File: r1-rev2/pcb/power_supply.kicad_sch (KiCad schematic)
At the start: 26 parts, among them J1 GT-BTP30003-xxxA-16A, Q1 AO3401A, U1 LM66100DCK, U2 TPS62A01DRLR, U3 TPS62A01DRLR, U4 TP4057, U5 XC6206P33xMR

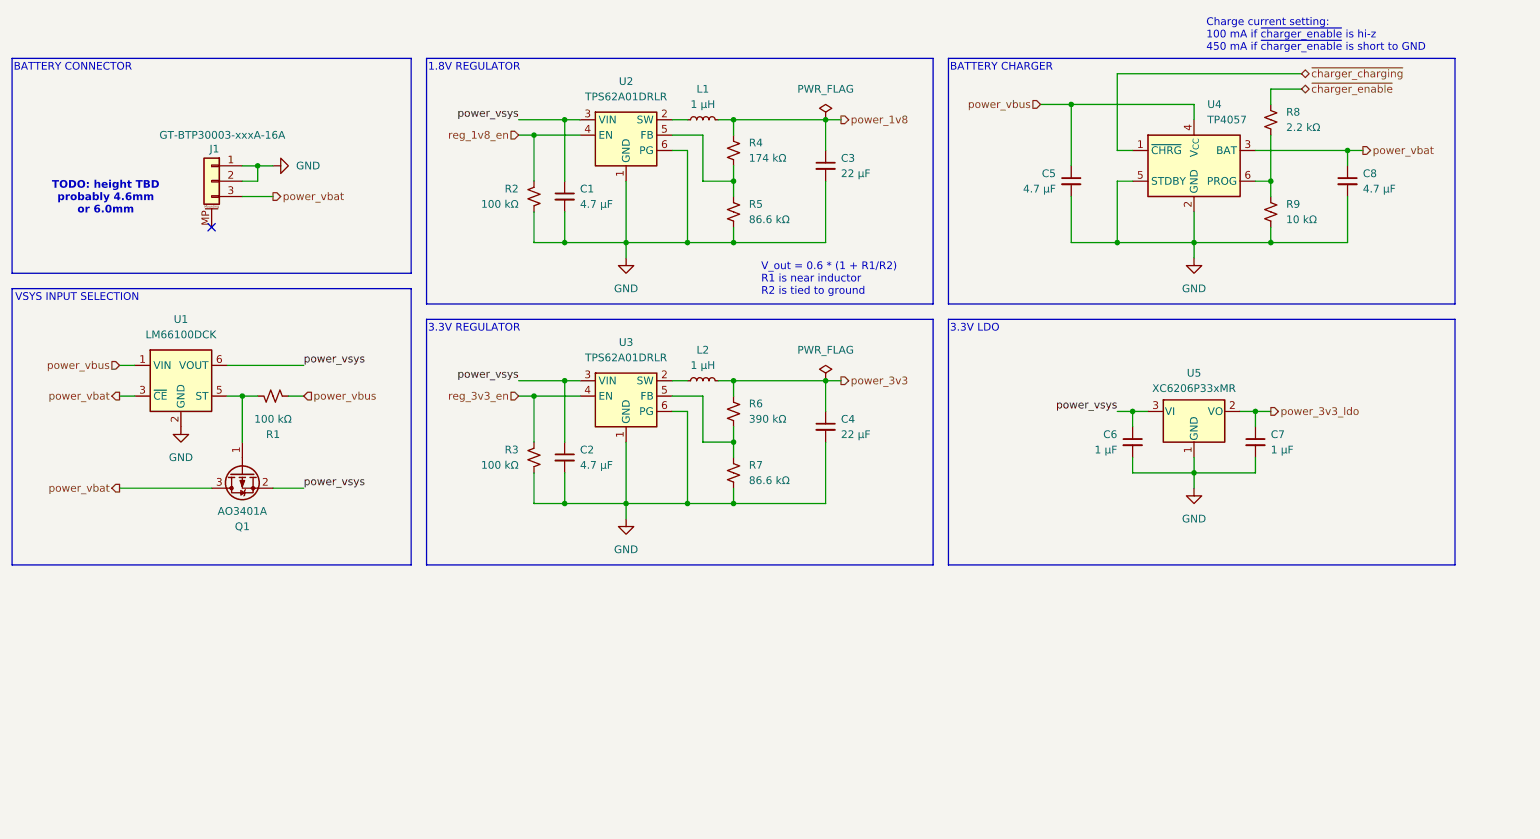
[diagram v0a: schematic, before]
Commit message: R1-Rev2: optimize resistor values
- Resistors used for the ADC dividers were way too high; I didn't
  take into account how the RC constant affected ADC performance
  so the conversion accuracy was probably poor. The new values are
  based on ST's recommendations and the theoretical resolution is
  computed in a spreadsheet.
- Simplify LO detect, originally I had the idea of a "wake on jack
  insert" feature but this is not possible for the headphone jack
  because it is only polled over I2C. The reason for the big 1M
  resistor that was there in Rev1 was to keep the effect on ground
  minimal. If the MCU is powered up then a simple hi-z input with
  internal pullup does the job better.
- Standardize on just 4 unique resistor values to reduce the cost
  of assembly: 5.1k is needed for USB, 2.2k for micbias and battery
  charge reference, and 15k and 68k for voltage reference. Other
  resistors have been rounded to one of these.
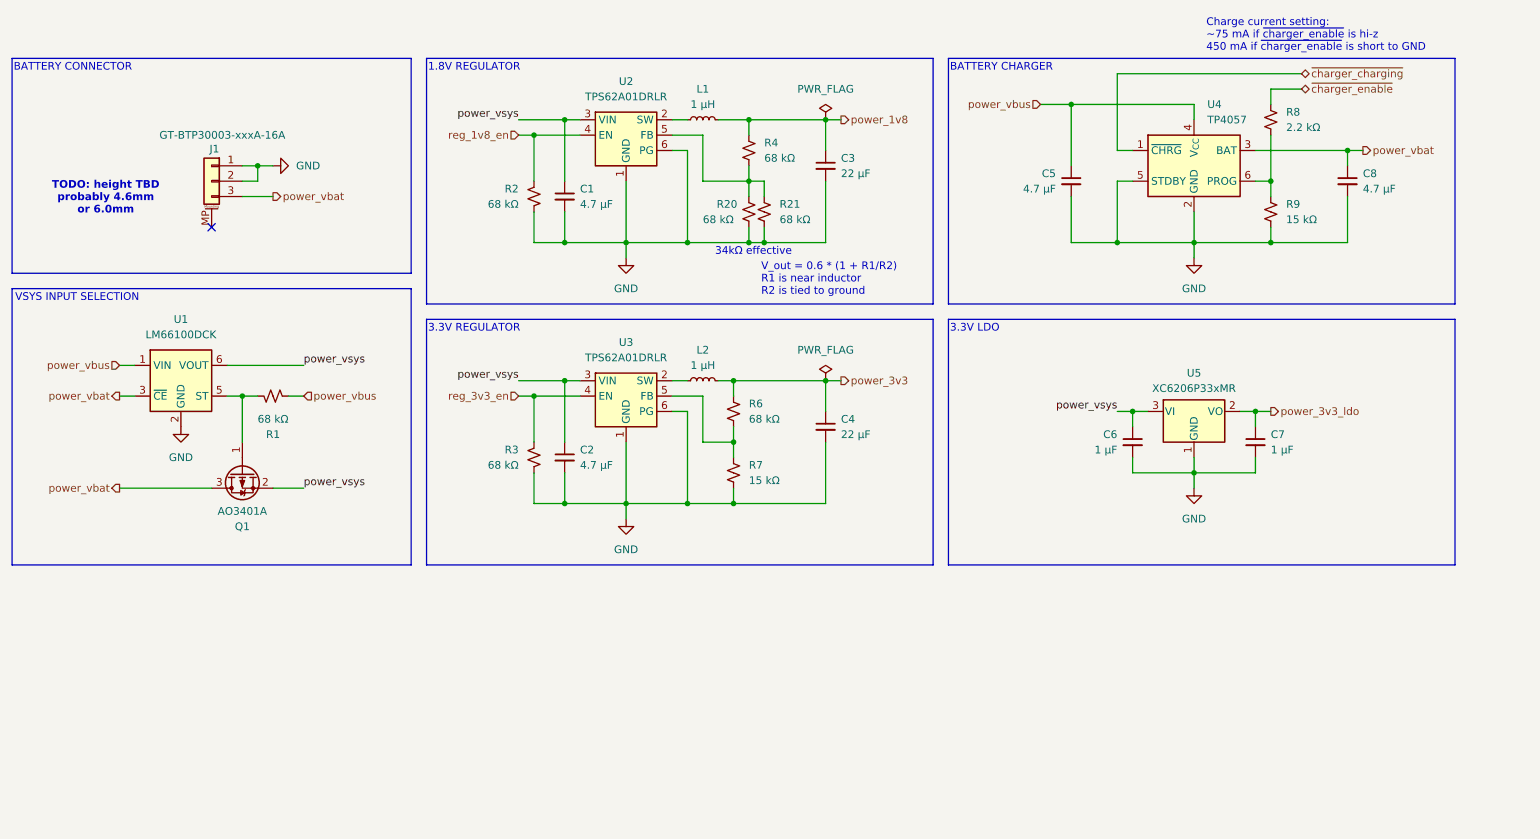
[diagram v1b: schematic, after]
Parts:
- removed R5: 86.6 kΩ, Resistor_SMD:R_0603_1608Metric, symbol Device:R_Small_US
- added R20, R21: 68 kΩ, Resistor_SMD:R_0603_1608Metric, symbol Device:R_Small_US
- R1, R2, R3: value 100 kΩ -> 68 kΩ
- R4: value 174 kΩ -> 68 kΩ
- R6: value 390 kΩ -> 68 kΩ
- R7: value 86.6 kΩ -> 15 kΩ
- R9: value 10 kΩ -> 15 kΩ
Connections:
- net GND: now also R20.2, R21.2
- net at R4.2, U2.5 (FB): now also R20.1, R21.1
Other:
- note added: "34kΩ effective"
- note added: "Charge current setting: ~75 mA if ~{charger_enable} is hi-z 450 mA if ~{charger_enable} is short to GND"
- note removed: "Charge current setting: 100 mA if ~{charger_enable} is hi-z 450 mA if ~{charger_enable} is short to GND"
- moved on the sheet: R4
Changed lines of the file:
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@@
 		)
 	)
+	(text "34kΩ effective"
+		(exclude_from_sim no)
+		(at 150.622 72.644 0)
+		(effects
+			(font
+				(size 1.27 1.27)
+			)
+		)
+	)
 	(text "V_out = 0.6 * (1 + R1/R2)\nR1 is near inductor\nR2 is tied to ground"
 		(exclude_from_sim no)
@@
 		)
 	)
-	(text "Charge current setting:\n100 mA if ~{charger_enable} is hi-z\n450 mA if ~{charger_enable} is short to GND"
+	(text "Charge current setting:\n~75 mA if ~{charger_enable} is hi-z\n450 mA if ~{charger_enable} is short to GND"
 		(exclude_from_sim no)
 		(at 225.552 36.83 0)
@@
 	)
 	(junction
-		(at 162.56 93.98)
+		(at 149.86 60.96)
 		(diameter 0)
 		(color 0 0 0 0)
 	)
 	(junction
-		(at 147.32 71.12)
+		(at 162.56 93.98)
 		(diameter 0)
 		(color 0 0 0 0)
@@
 	)
 	(junction
-		(at 147.32 50.8)
-		(diameter 0)
-		(color 0 0 0 0)
-	)
-	(junction
 		(at 147.32 93.98)
 		(diameter 0)
@@
 	)
 	(junction
+		(at 149.86 50.8)
+		(diameter 0)
+		(color 0 0 0 0)
+	)
+	(junction
 		(at 223.52 109.22)
 		(diameter 0)
@@
 	)
 	(junction
+		(at 149.86 71.12)
+		(diameter 0)
+		(color 0 0 0 0)
+	)
+	(junction
+		(at 152.4 71.12)
+		(diameter 0)
+		(color 0 0 0 0)
+	)
+	(junction
 		(at 129.54 71.12)
 		(diameter 0)
@@
 	)
 	(junction
-		(at 147.32 60.96)
-		(diameter 0)
-		(color 0 0 0 0)
-	)
-	(junction
 		(at 119.38 71.12)
 		(diameter 0)
@@
 	(wire
 		(pts
-			(xy 142.24 60.96) (xy 147.32 60.96)
+			(xy 142.24 60.96) (xy 149.86 60.96)
 		)
 		(stroke
@@
 	(wire
 		(pts
-			(xy 147.32 68.58) (xy 147.32 71.12)
+			(xy 149.86 68.58) (xy 149.86 71.12)
 		)
 		(stroke
@@
 	(wire
 		(pts
+			(xy 152.4 68.58) (xy 152.4 71.12)
+		)
+		(stroke
+			(width 0)
+			(type default)
+		)
+	)
+	(wire
+		(pts
 			(xy 147.32 104.14) (xy 147.32 106.68)
 		)
@@
 	(wire
 		(pts
+			(xy 152.4 60.96) (xy 152.4 63.5)
+		)
+		(stroke
+			(width 0)
+			(type default)
+		)
+	)
+	(wire
+		(pts
 			(xy 248.92 55.88) (xy 248.92 58.42)
 		)
@@
 	(wire
 		(pts
-			(xy 144.78 50.8) (xy 147.32 50.8)
+			(xy 144.78 50.8) (xy 149.86 50.8)
 		)
 		(stroke
@@
 	(wire
 		(pts
-			(xy 162.56 71.12) (xy 147.32 71.12)
+			(xy 162.56 71.12) (xy 152.4 71.12)
 		)
 		(stroke
@@
 	(wire
 		(pts
-			(xy 162.56 50.8) (xy 147.32 50.8)
+			(xy 162.56 50.8) (xy 149.86 50.8)
 		)
 		(stroke
@@
 	(wire
 		(pts
-			(xy 147.32 71.12) (xy 139.7 71.12)
+			(xy 139.7 71.12) (xy 149.86 71.12)
 		)
 		(stroke
@@
 	(wire
 		(pts
-			(xy 147.32 50.8) (xy 147.32 53.34)
+			(xy 149.86 50.8) (xy 149.86 53.34)
 		)
 		(stroke
@@
 	(wire
 		(pts
-			(xy 147.32 58.42) (xy 147.32 60.96)
+			(xy 149.86 58.42) (xy 149.86 60.96)
 		)
 		(stroke
@@
 	(wire
 		(pts
-			(xy 147.32 60.96) (xy 147.32 63.5)
+			(xy 149.86 60.96) (xy 149.86 63.5)
 		)
 		(stroke
@@
 	(wire
 		(pts
+			(xy 152.4 71.12) (xy 149.86 71.12)
+		)
+		(stroke
+			(width 0)
+			(type default)
+		)
+	)
+	(wire
+		(pts
 			(xy 210.82 99.06) (xy 213.36 99.06)
 		)
@@
 	(wire
 		(pts
+			(xy 149.86 60.96) (xy 152.4 60.96)
+		)
+		(stroke
+			(width 0)
+			(type default)
+		)
+	)
+	(wire
+		(pts
 			(xy 203.2 71.12) (xy 210.82 71.12)
 		)
@@
 			)
 		)
-		(property "Value" "100 kΩ"
+		(property "Value" "68 kΩ"
 			(at 111.76 64.7699 0)
 			(effects
@@
 			)
 		)
-		(property "Value" "10 kΩ"
+		(property "Value" "15 kΩ"
 			(at 238.76 67.3099 0)
 			(effects
@@
 	(symbol
 		(lib_id "Device:R_Small_US")
-		(at 147.32 66.04 0)
+		(at 149.86 66.04 0)
 		(unit 1)
 		(exclude_from_sim no)
@@
 		(on_board yes)
 		(dnp no)
-		(fields_autoplaced yes)
-		(property "Reference" "R5"
-			(at 149.86 64.7699 0)
+		(property "Reference" "R20"
+			(at 144.526 64.77 0)
 			(effects
 				(font
@@
 			)
 		)
-		(property "Value" "86.6 kΩ"
-			(at 149.86 67.3099 0)
+		(property "Value" "68 kΩ"
+			(at 142.24 67.3101 0)
 			(effects
 				(font
@@
 		)
 		(property "Footprint" "Resistor_SMD:R_0603_1608Metric"
-			(at 147.32 66.04 0)
+			(at 149.86 66.04 0)
 			(effects
 				(font
@@
 		)
 		(property "Datasheet" "~"
-			(at 147.32 66.04 0)
+			(at 149.86 66.04 0)
 			(effects
 				(font
@@
 		)
 		(property "Description" "Resistor, small US symbol"
-			(at 147.32 66.04 0)
+			(at 149.86 66.04 0)
 			(effects
 				(font
@@
 			)
 		)
-		(property "LCSC#" "C3000725"
-			(at 147.32 66.04 0)
+		(property "LCSC#" "C2933159"
+			(at 149.86 66.04 0)
 			(effects
 				(font
@@
 			(project "echo-r1"
 				(path "/aa241847-30f4-429d-a148-6a6e39ba98e0/48d39f5c-11a4-46cd-927a-56a9c6ae42fa"
-					(reference "R5")
+					(reference "R20")
 					(unit 1)
 				)
@@
 	)
 	(symbol
+		(lib_id "Device:R_Small_US")
+		(at 152.4 66.04 0)
+		(unit 1)
+		(exclude_from_sim no)
+		(in_bom yes)
+		(on_board yes)
+		(dnp no)
+		(fields_autoplaced yes)
+		(property "Reference" "R21"
+			(at 154.94 64.7699 0)
+			(effects
+				(font
+					(size 1.27 1.27)
+				)
+				(justify left)
+			)
+		)
+		(property "Value" "68 kΩ"
+			(at 154.94 67.3099 0)
+			(effects
+				(font
+					(size 1.27 1.27)
+				)
+				(justify left)
+			)
+		)
+		(property "Footprint" "Resistor_SMD:R_0603_1608Metric"
+			(at 152.4 66.04 0)
+			(effects
+				(font
+					(size 1.27 1.27)
+				)
+				(hide yes)
+			)
+		)
+		(property "Datasheet" "~"
+			(at 152.4 66.04 0)
+			(effects
+				(font
+					(size 1.27 1.27)
+				)
+				(hide yes)
+			)
+		)
+		(property "Description" "Resistor, small US symbol"
+			(at 152.4 66.04 0)
+			(effects
+				(font
+					(size 1.27 1.27)
+				)
+				(hide yes)
+			)
+		)
+		(property "LCSC#" "C2933159"
+			(at 152.4 66.04 0)
+			(effects
+				(font
+					(size 1.27 1.27)
+				)
+				(hide yes)
+			)
+		)
+		(pin "2"
+		)
+		(pin "1"
+		)
+		(instances
+			(project "echo-r1"
+				(path "/aa241847-30f4-429d-a148-6a6e39ba98e0/48d39f5c-11a4-46cd-927a-56a9c6ae42fa"
+					(reference "R21")
+					(unit 1)
+				)
+			)
+		)
+	)
+	(symbol
 		(lib_id "power:GND")
 		(at 223.52 111.76 0)
@@
 			)
 		)
-		(property "Value" "100 kΩ"
+		(property "Value" "68 kΩ"
 			(at 111.76 107.9499 0)
 			(effects
@@
 			)
 		)
-		(property "Value" "86.6 kΩ"
+		(property "Value" "15 kΩ"
 			(at 149.86 110.4899 0)
 			(effects
@@
 			)
 		)
-		(property "Value" "390 kΩ"
+		(property "Value" "68 kΩ"
 			(at 149.86 100.3299 0)
 			(effects
@@
 	(symbol
 		(lib_id "Device:R_Small_US")
-		(at 147.32 55.88 0)
+		(at 149.86 55.88 0)
 		(unit 1)
 		(exclude_from_sim no)
@@
 		(fields_autoplaced yes)
 		(property "Reference" "R4"
-			(at 149.86 54.6099 0)
+			(at 152.4 54.6099 0)
 			(effects
 				(font
@@
 			)
 		)
-		(property "Value" "174 kΩ"
-			(at 149.86 57.1499 0)
+		(property "Value" "68 kΩ"
+			(at 152.4 57.1499 0)
 			(effects
 				(font
@@
 		)
 		(property "Footprint" "Resistor_SMD:R_0603_1608Metric"
-			(at 147.32 55.88 0)
+			(at 149.86 55.88 0)
 			(effects
 				(font
@@
 		)
 		(property "Datasheet" "~"
-			(at 147.32 55.88 0)
+			(at 149.86 55.88 0)
 			(effects
 				(font
@@
 		)
 		(property "Description" "Resistor, small US symbol"
-			(at 147.32 55.88 0)
+			(at 149.86 55.88 0)
 			(effects
 				(font
@@
 		)
 		(property "LCSC#" "C2933159"
-			(at 147.32 55.88 0)
+			(at 149.86 55.88 0)
 			(effects
 				(font
@@
 			)
 		)
-		(property "Value" "100 kΩ"
+		(property "Value" "68 kΩ"
 			(at 71.12 100.33 90)
 			(effects

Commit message: R1-Rev2: strip LCSC part numbers from schematic
These will be managed in a separate BOM spreadsheet going forward.
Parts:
- C1, C2, C3, C4: LCSC# C86816 -> (none)
- C5, C8: LCSC# C69335 -> (none)
- C6, C7: LCSC# C52923 -> (none)
- J1: LCSC# C41378737 -> (none)
- L1, L2: LCSC# C161082 -> (none)
- Q1: LCSC# C347476 -> (none)
- R1, R2, R3: LCSC# C60491 -> (none)
- R20, R21, R4: LCSC# C2933159 -> (none)
- R6: LCSC# C23150 -> (none)
- R7: LCSC# C3000725 -> (none)
- R8: LCSC# C114762 -> (none)
- R9: LCSC# C60490 -> (none)
- U1: LCSC# C2869734 -> (none)
- U2, U3: LCSC# C5157937 -> (none)
- U4: LCSC# C725791 -> (none)
- U5: LCSC# C5446 -> (none)

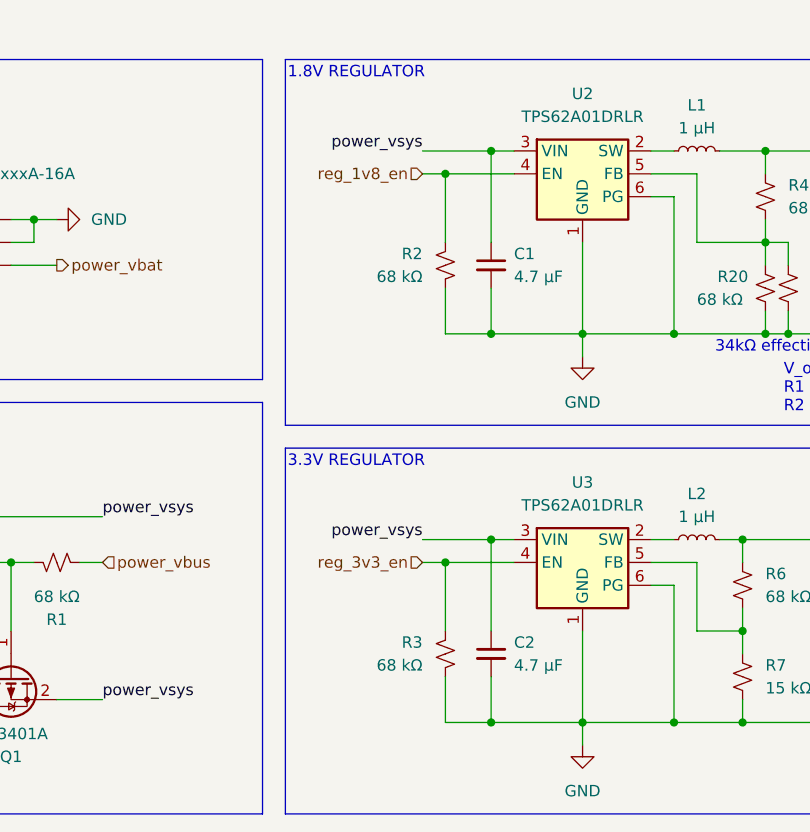
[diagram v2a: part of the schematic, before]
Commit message: R1-Rev2: add debouncing for regulator enable signal
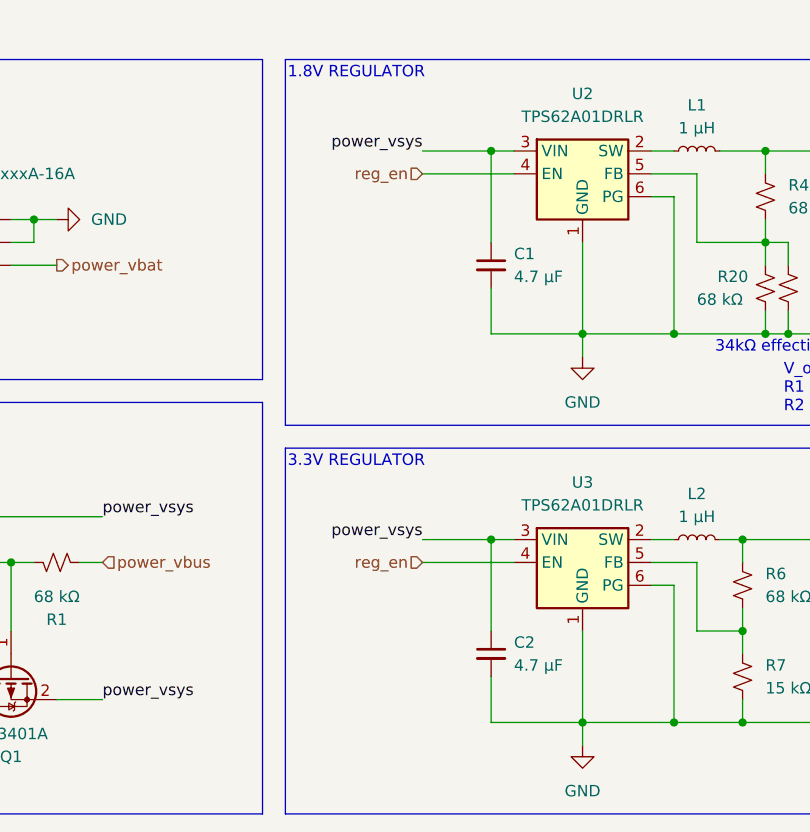
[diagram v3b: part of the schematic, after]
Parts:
- removed R2, R3: 68 kΩ, Resistor_SMD:R_0402_1005Metric, symbol Device:R_Small_US
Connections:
- net reg_3v3_en is gone; now on net reg_en: U3.4 (EN)
- net reg_1v8_en renamed reg_en
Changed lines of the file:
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@@
-	)
-	(junction
-		(at 119.38 71.12)
-		(diameter 0)
-		(color 0 0 0 0)
 	)
 	(junction
@@
 	)
 	(junction
-		(at 119.38 114.3)
-		(diameter 0)
-		(color 0 0 0 0)
-	)
-	(junction
 		(at 223.52 71.12)
 		(diameter 0)
@@
 		(color 0 0 0 0)
 	)
-	(junction
-		(at 114.3 53.34)
-		(diameter 0)
-		(color 0 0 0 0)
-	)
-	(junction
-		(at 114.3 96.52)
-		(diameter 0)
-		(color 0 0 0 0)
-	)
 	(no_connect
 		(at 60.96 68.58)
@@
 	(wire
 		(pts
-			(xy 111.76 53.34) (xy 114.3 53.34)
-		)
-		(stroke
-			(width 0)
-			(type default)
-		)
-	)
-	(wire
-		(pts
 			(xy 142.24 53.34) (xy 137.16 53.34)
 		)
@@
 	(wire
 		(pts
-			(xy 114.3 114.3) (xy 119.38 114.3)
-		)
-		(stroke
-			(width 0)
-			(type default)
-		)
-	)
-	(wire
-		(pts
 			(xy 162.56 93.98) (xy 165.1 93.98)
 		)
@@
 	(wire
 		(pts
-			(xy 111.76 96.52) (xy 114.3 96.52)
-		)
-		(stroke
-			(width 0)
-			(type default)
-		)
-	)
-	(wire
-		(pts
 			(xy 203.2 63.5) (xy 203.2 71.12)
 		)
@@
 	(wire
 		(pts
-			(xy 114.3 71.12) (xy 119.38 71.12)
-		)
-		(stroke
-			(width 0)
-			(type default)
-		)
-	)
-	(wire
-		(pts
 			(xy 162.56 50.8) (xy 149.86 50.8)
 		)
@@
 	(wire
 		(pts
-			(xy 114.3 96.52) (xy 121.92 96.52)
+			(xy 111.76 96.52) (xy 121.92 96.52)
 		)
 		(stroke
@@
 	(wire
 		(pts
-			(xy 114.3 96.52) (xy 114.3 104.14)
-		)
-		(stroke
-			(width 0)
-			(type default)
-		)
-	)
-	(wire
-		(pts
 			(xy 137.16 55.88) (xy 139.7 55.88)
 		)
@@
 	(wire
 		(pts
-			(xy 114.3 53.34) (xy 114.3 60.96)
-		)
-		(stroke
-			(width 0)
-			(type default)
-		)
-	)
-	(wire
-		(pts
 			(xy 68.58 58.42) (xy 71.12 58.42)
 		)
@@
 	(wire
 		(pts
-			(xy 114.3 109.22) (xy 114.3 114.3)
-		)
-		(stroke
-			(width 0)
-			(type default)
-		)
-	)
-	(wire
-		(pts
 			(xy 198.12 48.26) (xy 203.2 48.26)
 		)
@@
 	(wire
 		(pts
-			(xy 114.3 66.04) (xy 114.3 71.12)
-		)
-		(stroke
-			(width 0)
-			(type default)
-		)
-	)
-	(wire
-		(pts
 			(xy 147.32 101.6) (xy 147.32 104.14)
 		)
@@
 	(wire
 		(pts
-			(xy 114.3 53.34) (xy 121.92 53.34)
+			(xy 111.76 53.34) (xy 121.92 53.34)
 		)
 		(stroke
@@
 		)
 	)
-	(hierarchical_label "reg_3v3_en"
+	(hierarchical_label "reg_en"
 		(shape input)
 		(at 111.76 96.52 180)
@@
 		)
 	)
-	(hierarchical_label "reg_1v8_en"
+	(hierarchical_label "reg_en"
 		(shape input)
 		(at 111.76 53.34 180)
@@
 	)
 	(symbol
-		(lib_id "Device:R_Small_US")
-		(at 114.3 63.5 0)
-		(mirror y)
-		(unit 1)
-		(exclude_from_sim no)
-		(in_bom yes)
-		(on_board yes)
-		(dnp no)
-		(property "Reference" "R2"
-			(at 111.76 62.2299 0)
-			(effects
-				(font
-					(size 1.27 1.27)
-				)
-				(justify left)
-			)
-		)
-		(property "Value" "68 kΩ"
-			(at 111.76 64.7699 0)
-			(effects
-				(font
-					(size 1.27 1.27)
-				)
-				(justify left)
-			)
-		)
-		(property "Footprint" "Resistor_SMD:R_0402_1005Metric"
-			(at 114.3 63.5 0)
-			(effects
-				(font
-					(size 1.27 1.27)
-				)
-				(hide yes)
-			)
-		)
-		(property "Datasheet" "~"
-			(at 114.3 63.5 0)
-			(effects
-				(font
-					(size 1.27 1.27)
-				)
-				(hide yes)
-			)
-		)
-		(property "Description" "Resistor, small US symbol"
-			(at 114.3 63.5 0)
-			(effects
-				(font
-					(size 1.27 1.27)
-				)
-				(hide yes)
-			)
-		)
-		(pin "2"
-		)
-		(pin "1"
-		)
-		(instances
-			(project "echo-r1"
-				(path "/aa241847-30f4-429d-a148-6a6e39ba98e0/48d39f5c-11a4-46cd-927a-56a9c6ae42fa"
-					(reference "R2")
-					(unit 1)
-				)
-			)
-		)
-	)
-	(symbol
 		(lib_id "Battery_Management:TP4057")
 		(at 223.52 58.42 0)
@@
 					(unit 1)
 				)
-			)
-		)
-	)
-	(symbol
-		(lib_id "Device:R_Small_US")
-		(at 114.3 106.68 0)
-		(mirror y)
-		(unit 1)
-		(exclude_from_sim no)
-		(in_bom yes)
-		(on_board yes)
-		(dnp no)
-		(property "Reference" "R3"
-			(at 111.76 105.4099 0)
-			(effects
-				(font
-					(size 1.27 1.27)
-				)
-				(justify left)
-			)
-		)
-		(property "Value" "68 kΩ"
-			(at 111.76 107.9499 0)
-			(effects
-				(font
-					(size 1.27 1.27)
-				)
-				(justify left)
-			)
-		)
-		(property "Footprint" "Resistor_SMD:R_0402_1005Metric"
-			(at 114.3 106.68 0)
-			(effects
-				(font
-					(size 1.27 1.27)
-				)
-				(hide yes)
-			)
-		)
-		(property "Datasheet" "~"
-			(at 114.3 106.68 0)
-			(effects
-				(font
-					(size 1.27 1.27)
-				)
-				(hide yes)
-			)
-		)
-		(property "Description" "Resistor, small US symbol"
-			(at 114.3 106.68 0)
-			(effects
-				(font
-					(size 1.27 1.27)
-				)
-				(hide yes)
-			)
-		)
-		(pin "2"
-		)
-		(pin "1"
-		)
-		(instances
-			(project "echo-r1"
-				(path "/aa241847-30f4-429d-a148-6a6e39ba98e0/48d39f5c-11a4-46cd-927a-56a9c6ae42fa"
-					(reference "R3")
-					(unit 1)
-				)
